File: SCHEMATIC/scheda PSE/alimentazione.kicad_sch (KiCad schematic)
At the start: 33 parts

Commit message: prova librerie
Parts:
- removed D?: S1B, symbol Device:D
- added D?: RBR1VWM30ATFTR, symbol Device:D_Schottky
- U?: farnell (none) -> 4144775
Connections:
- net +5V: now also D?.2 (A)
- net VOUT_5V: now also D?.1 (K)
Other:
- moved on the sheet: D?
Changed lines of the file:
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@@
   (junction (at 196.85 54.61) (diameter 0) (color 0 0 0 0)
   )
-  (junction (at 253.365 95.885) (diameter 0) (color 0 0 0 0)
+  (junction (at 249.555 95.885) (diameter 0) (color 0 0 0 0)
   )
   (junction (at 217.17 95.885) (diameter 0) (color 0 0 0 0)
@@
     (stroke (width 0) (type default) (color 0 0 0 0))
   )
-  (wire (pts (xy 254.635 95.885) (xy 253.365 95.885))
+  (wire (pts (xy 254.635 95.885) (xy 249.555 95.885))
     (stroke (width 0) (type default) (color 0 0 0 0))
   )
@@
     (stroke (width 0) (type default) (color 0 0 0 0))
   )
-  (wire (pts (xy 253.365 95.885) (xy 253.365 95.25))
+  (wire (pts (xy 249.555 95.885) (xy 249.555 95.25))
     (stroke (width 0) (type default) (color 0 0 0 0))
   )
@@
     (stroke (width 0) (type default) (color 0 0 0 0))
   )
-  (wire (pts (xy 67.945 95.885) (xy 73.66 95.885))
-    (stroke (width 0) (type default) (color 0 0 0 0))
-  )
-  (wire (pts (xy 247.015 95.885) (xy 253.365 95.885))
+  (wire (pts (xy 66.04 95.885) (xy 73.66 95.885))
+    (stroke (width 0) (type default) (color 0 0 0 0))
+  )
+  (wire (pts (xy 247.015 95.885) (xy 249.555 95.885))
     (stroke (width 0) (type default) (color 0 0 0 0))
   )
@@
     (stroke (width 0) (type default) (color 0 0 0 0))
   )
-  (wire (pts (xy 48.26 95.885) (xy 60.325 95.885))
+  (wire (pts (xy 48.26 95.885) (xy 58.42 95.885))
     (stroke (width 0) (type default) (color 0 0 0 0))
   )
@@
     (effects (font (size 1.27 1.27)) (justify left bottom))
   )
-  (label "VBUS" (at 83.82 52.705 0)
+  (label "VBUS" (at 84.455 52.705 0)
     (effects (font (size 1.27 1.27)) (justify left bottom))
   )
@@
     (effects (font (size 1.27 1.27)) (justify left bottom))
   )
-  (label "VIN_ POST_PPTC" (at 45.085 95.885 0)
+  (label "VIN_ POST_PPTC" (at 44.45 95.885 0)
     (effects (font (size 1.27 1.27)) (justify left bottom))
   )
@@
     (pin "1")
   )
-  (symbol (lib_id "power:+5V") (at 253.365 95.25 0) (unit 1)
-    (in_bom yes) (on_board yes) (fields_autoplaced)
-    (property "Reference" "#PWR0146" (id 0) (at 253.365 99.06 0)
-      (effects (font (size 1.27 1.27)) hide)
-    )
-    (property "Value" "+5V" (id 1) (at 253.365 91.6742 0))
-    (property "Footprint" "" (id 2) (at 253.365 95.25 0)
-      (effects (font (size 1.27 1.27)) hide)
-    )
-    (property "Datasheet" "" (id 3) (at 253.365 95.25 0)
+  (symbol (lib_id "power:+5V") (at 249.555 95.25 0) (unit 1)
+    (in_bom yes) (on_board yes) (fields_autoplaced)
+    (property "Reference" "#PWR0146" (id 0) (at 249.555 99.06 0)
+      (effects (font (size 1.27 1.27)) hide)
+    )
+    (property "Value" "+5V" (id 1) (at 249.555 91.6742 0))
+    (property "Footprint" "" (id 2) (at 249.555 95.25 0)
+      (effects (font (size 1.27 1.27)) hide)
+    )
+    (property "Datasheet" "" (id 3) (at 249.555 95.25 0)
       (effects (font (size 1.27 1.27)) hide)
     )
@@
     (pin "1")
   )
+  (symbol (lib_id "Device:D_Schottky") (at 258.445 95.885 180) (unit 1)
+    (in_bom yes) (on_board yes)
+    (property "Reference" "D?" (id 0) (at 258.445 93.345 0))
+    (property "Value" "RBR1VWM30ATFTR" (id 1) (at 260.35 99.06 0))
+    (property "Footprint" "" (id 2) (at 258.445 95.885 0)
+      (effects (font (size 1.27 1.27)) hide)
+    )
+    (property "Datasheet" "~" (id 3) (at 258.445 95.885 0)
+      (effects (font (size 1.27 1.27)) hide)
+    )
+    (pin "1")
+    (pin "2")
+  )
   (symbol (lib_id "power:GND") (at 177.165 113.665 0) (unit 1)
     (in_bom yes) (on_board yes) (fields_autoplaced)
@@
   (symbol (lib_id "Connector:TestPoint") (at 196.85 53.975 0) (unit 1)
     (in_bom yes) (on_board yes)
-    (property "Reference" "TP?" (id 0) (at 195.58 48.895 0)
-      (effects (font (size 1.27 1.27)) (justify left))
-    )
-    (property "Value" "3V3" (id 1) (at 195.58 46.3581 0)
+    (property "Reference" "TP?" (id 0) (at 198.12 50.8 0)
+      (effects (font (size 1.27 1.27)) (justify left))
+    )
+    (property "Value" "3V3" (id 1) (at 198.12 48.895 0)
       (effects (font (size 1.27 1.27)) (justify left))
     )
@@
       (effects (font (size 1.27 1.27)) hide)
     )
+    (property "farnell" "4144775" (id 4) (at 171.45 54.61 0)
+      (effects (font (size 1.27 1.27)) hide)
+    )
     (pin "1")
     (pin "2")
@@
     (pin "2")
   )
-  (symbol (lib_id "Device:D") (at 64.135 95.885 180) (unit 1)
-    (in_bom yes) (on_board yes) (fields_autoplaced)
-    (property "Reference" "D?" (id 0) (at 64.135 90.9152 0))
-    (property "Value" "S1B" (id 1) (at 64.135 93.4521 0))
-    (property "Footprint" "" (id 2) (at 64.135 95.885 0)
-      (effects (font (size 1.27 1.27)) hide)
-    )
-    (property "Datasheet" "~" (id 3) (at 64.135 95.885 0)
+  (symbol (lib_id "Device:D") (at 62.23 95.885 180) (unit 1)
+    (in_bom yes) (on_board yes)
+    (property "Reference" "D?" (id 0) (at 62.23 90.1731 0))
+    (property "Value" "S1B" (id 1) (at 62.23 92.71 0))
+    (property "Footprint" "" (id 2) (at 62.23 95.885 0)
+      (effects (font (size 1.27 1.27)) hide)
+    )
+    (property "Datasheet" "~" (id 3) (at 62.23 95.885 0)
       (effects (font (size 1.27 1.27)) hide)
     )
@@
   (symbol (lib_id "Device:Polyfuse") (at 40.64 95.885 90) (unit 1)
     (in_bom yes) (on_board yes)
-    (property "Reference" "F?" (id 0) (at 40.64 90.7882 90))
-    (property "Value" "2016L05MR" (id 1) (at 40.64 93.3251 90))
+    (property "Reference" "F?" (id 0) (at 40.64 90.1731 90))
+    (property "Value" "2016L05MR" (id 1) (at 40.64 92.71 90))
     (property "Footprint" "" (id 2) (at 45.72 94.615 0)
       (effects (font (size 1.27 1.27)) (justify left) hide)
@@
     (pin "1")
   )
-  (symbol (lib_id "Device:D") (at 258.445 95.885 180) (unit 1)
-    (in_bom yes) (on_board yes) (fields_autoplaced)
-    (property "Reference" "D?" (id 0) (at 258.445 90.9152 0))
-    (property "Value" "S1B" (id 1) (at 258.445 93.4521 0))
-    (property "Footprint" "" (id 2) (at 258.445 95.885 0)
-      (effects (font (size 1.27 1.27)) hide)
-    )
-    (property "Datasheet" "~" (id 3) (at 258.445 95.885 0)
-      (effects (font (size 1.27 1.27)) hide)
-    )
-    (pin "1")
-    (pin "2")
-  )
   (symbol (lib_id "Device:R") (at 247.015 109.855 0) (unit 1)

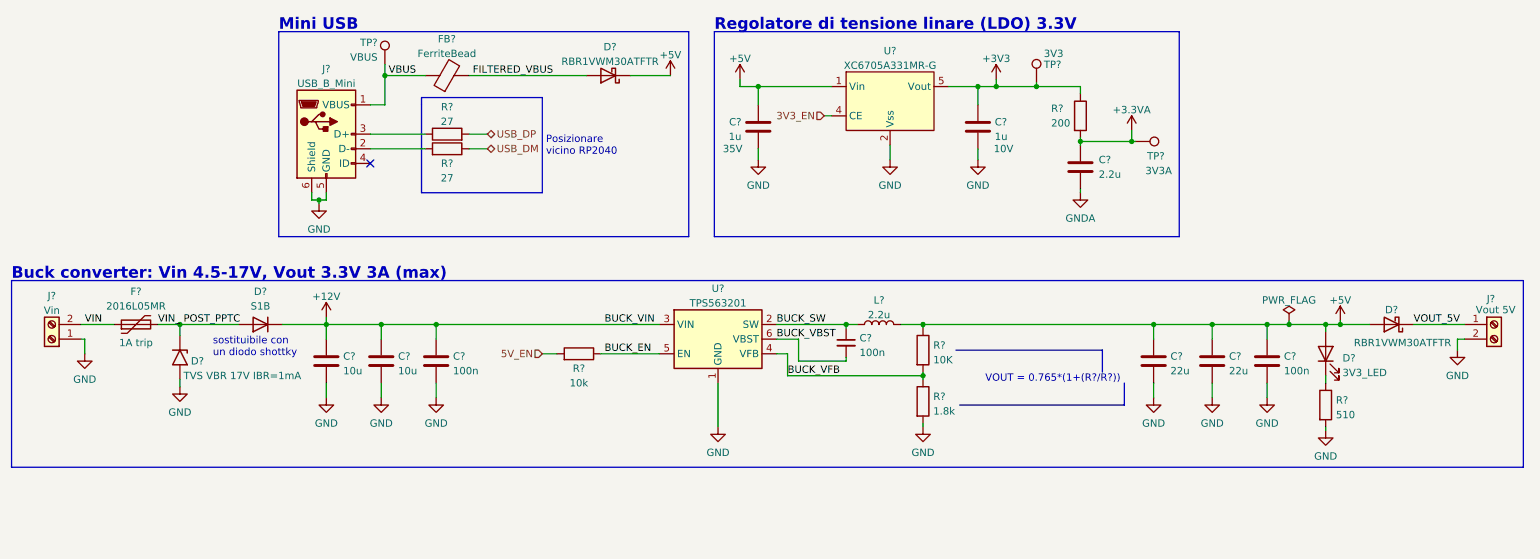
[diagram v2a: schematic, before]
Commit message: Aggiunti QUASI tutti i footprint
aggiunti quasi tutti i footprint dei componenti
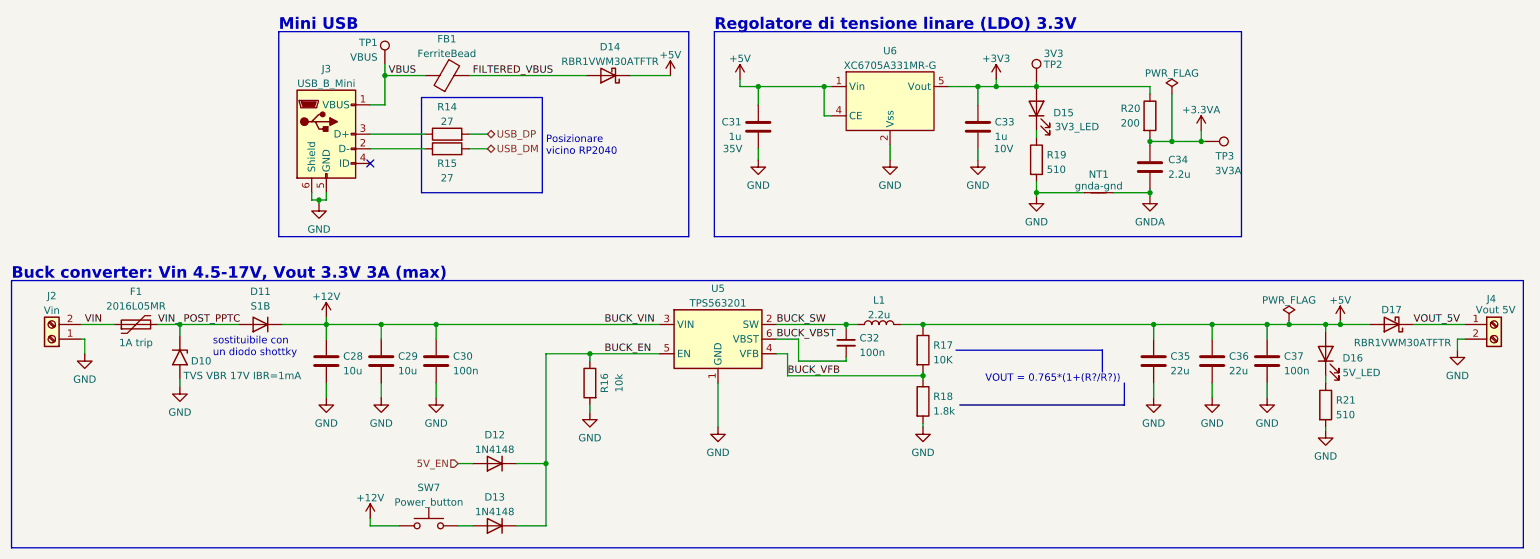
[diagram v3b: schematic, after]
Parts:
- added D12, D13: 1N4148, Diode_SMD:D_SOD-123, symbol Diode:1N4148
- added D15: 3V3_LED, LED_SMD:LED_0603_1608Metric, symbol Device:LED
- added NT1: gnda-gnd, NetTie:NetTie-2_SMD_Pad0.5mm, symbol Device:NetTie_2
- added R19: 510, Resistor_SMD:R_0603_1608Metric, symbol Device:R
- added SW7: Power_button, Button_Switch_THT:SW_PUSH_6mm_H5mm, symbol Switch:SW_Push
- C28, C29, C35, C36: renamed from C?; footprint (none) -> Capacitor_SMD:C_0805_2012Metric
- C30, C31, C32, C33, C34, C37: renamed from C?; footprint (none) -> Capacitor_SMD:C_0603_1608Metric
- D16: renamed from D?; value 3V3_LED -> 5V_LED; footprint (none) -> LED_SMD:LED_0603_1608Metric
- J2, J4: renamed from J?; footprint (none) -> TerminalBlock:TerminalBlock_bornier-2_P5.08mm
- R14, R15, R16, R17, R18, R20, R21: renamed from R?; footprint (none) -> Resistor_SMD:R_0603_1608Metric
- TP1, TP2, TP3: renamed from TP?; footprint (none) -> TestPoint:TestPoint_Loop_D2.50mm_Drill1.0mm_LowProfile
- gave numbers to parts that had none: 10
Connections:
- net 3V3_EN is gone; now on net +5V: U6.4 (CE)
- net +12V: now also SW7.1
- net +3V3: now also D15.2 (A)
- net 5V_EN: now also D12.2 (A); no longer R16.2
- net BUCK_EN: now also D12.1 (K), D13.1 (K)
- net GND: now also R16.2, NT1.1, R19.2
- net GNDA: now also NT1.2
- new net: D13.2 (A), SW7.2
- new net: D15.1 (K), R19.1
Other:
- moved on the sheet: C34, R16, R20, TP3

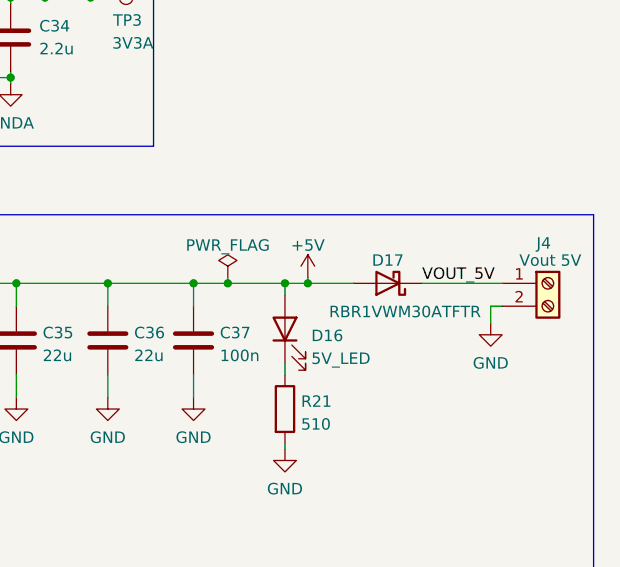
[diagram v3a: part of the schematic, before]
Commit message: iniziato il layout, posizionati componenti principali
incominciato il posizionamento dei componenti nel layout. Sono stati posizionati i componenti principali come led RGB, GPS, schermo, pulsanti vari, buzzer
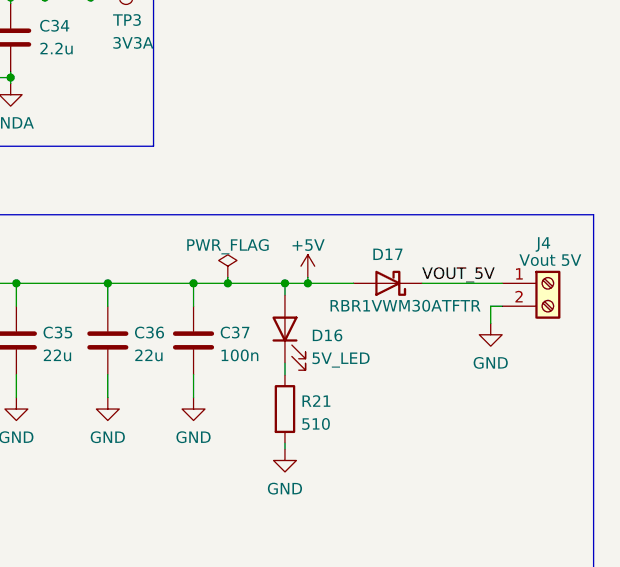
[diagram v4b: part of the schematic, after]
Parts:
- D10: footprint Diode_THT:D_DO-201AE_P15.24mm_Horizontal -> Diode_SMD:D_SMA; mouser (none) -> 576-SMAJ15A
- D11: footprint (none) -> Diode_SMD:D_SMA; farnell (none) -> 2675037
- D14, D17: footprint (none) -> Diode_SMD:D_SOD-123; farnell (none) -> 2311223
- D15, D16: footprint LED_SMD:LED_0603_1608Metric -> LED_SMD:LED_0805_2012Metric
- F1: footprint (none) -> Fuse:Fuse_1206_3216Metric; farnell (none) -> 1652159
- FB1: footprint (none) -> Capacitor_SMD:C_0805_2012Metric; farnell (none) -> 1515661
- J3: footprint (none) -> _PSE:USB mini
- L1: footprint (none) -> _PSE:IHLP1212BZER2R2M11; farnell (none) -> 2056527
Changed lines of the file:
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@@
     (pin "1")
-  )
-  (symbol (lib_id "Device:D_Schottky") (at 258.445 95.885 180) (unit 1)
-    (in_bom yes) (on_board yes)
-    (property "Reference" "D17" (id 0) (at 258.445 93.345 0))
-    (property "Value" "RBR1VWM30ATFTR" (id 1) (at 260.35 99.06 0))
-    (property "Footprint" "" (id 2) (at 258.445 95.885 0)
-      (effects (font (size 1.27 1.27)) hide)
-    )
-    (property "Datasheet" "~" (id 3) (at 258.445 95.885 0)
-      (effects (font (size 1.27 1.27)) hide)
-    )
-    (pin "1")
-    (pin "2")
   )
   (symbol (lib_id "power:GND") (at 177.165 113.665 0) (unit 1)
@@
     (pin "1")
   )
+  (symbol (lib_id "Device:D_Schottky") (at 258.445 95.885 180) (unit 1)
+    (in_bom yes) (on_board yes)
+    (property "Reference" "D17" (id 0) (at 258.445 92.71 0))
+    (property "Value" "RBR1VWM30ATFTR" (id 1) (at 260.35 98.425 0))
+    (property "Footprint" "Diode_SMD:D_SOD-123" (id 2) (at 258.445 95.885 0)
+      (effects (font (size 1.27 1.27)) hide)
+    )
+    (property "Datasheet" "https://4donline.ihs.com/images/VipMasterIC/IC/NEXP/NEXP-S-A0003060256/NEXP-S-A0003059924-1.pdf?hkey=6D3A4C79FDBF58556ACFDE234799DDF0" (id 3) (at 258.445 95.885 0)
+      (effects (font (size 1.27 1.27)) hide)
+    )
+    (property "farnell" "2311223" (id 4) (at 258.445 95.885 0)
+      (effects (font (size 1.27 1.27)) hide)
+    )
+    (pin "1")
+    (pin "2")
+  )
   (symbol (lib_id "Connector:Screw_Terminal_01x02") (at 276.225 95.885 0) (unit 1)
     (in_bom yes) (on_board yes)
@@
     (property "Reference" "D11" (id 0) (at 62.23 90.1731 0))
     (property "Value" "S1B" (id 1) (at 62.23 92.71 0))
-    (property "Footprint" "" (id 2) (at 62.23 95.885 0)
-      (effects (font (size 1.27 1.27)) hide)
-    )
-    (property "Datasheet" "~" (id 3) (at 62.23 95.885 0)
+    (property "Footprint" "Diode_SMD:D_SMA" (id 2) (at 62.23 95.885 0)
+      (effects (font (size 1.27 1.27)) hide)
+    )
+    (property "Datasheet" "https://www.farnell.com/datasheets/2863963.pdf" (id 3) (at 62.23 95.885 0)
+      (effects (font (size 1.27 1.27)) hide)
+    )
+    (property "farnell" "2675037" (id 4) (at 62.23 95.885 0)
       (effects (font (size 1.27 1.27)) hide)
     )
@@
     (property "Reference" "F1" (id 0) (at 40.64 90.1731 90))
     (property "Value" "2016L05MR" (id 1) (at 40.64 92.71 90))
-    (property "Footprint" "" (id 2) (at 45.72 94.615 0)
+    (property "Footprint" "Fuse:Fuse_1206_3216Metric" (id 2) (at 45.72 94.615 0)
       (effects (font (size 1.27 1.27)) (justify left) hide)
     )
-    (property "Datasheet" "~" (id 3) (at 40.64 95.885 0)
+    (property "Datasheet" "https://www.farnell.com/datasheets/2360307.pdf" (id 3) (at 40.64 95.885 0)
       (effects (font (size 1.27 1.27)) hide)
     )
     (property "Rating" "1A trip" (id 4) (at 40.64 99.06 90))
+    (property "farnell" "1652159" (id 5) (at 40.64 95.885 90)
+      (effects (font (size 1.27 1.27)) hide)
+    )
     (pin "1")
     (pin "2")
@@
       (effects (font (size 1.27 1.27)) (justify right))
     )
-    (property "Footprint" "LED_SMD:LED_0603_1608Metric" (id 2) (at 196.85 58.42 0)
+    (property "Footprint" "LED_SMD:LED_0805_2012Metric" (id 2) (at 196.85 58.42 0)
       (effects (font (size 1.27 1.27)) hide)
     )
@@
     (property "Reference" "L1" (id 0) (at 169.545 91.6772 90))
     (property "Value" "2.2u" (id 1) (at 169.545 94.2141 90))
-    (property "Footprint" "" (id 2) (at 169.545 95.885 0)
-      (effects (font (size 1.27 1.27)) hide)
-    )
-    (property "Datasheet" "~" (id 3) (at 169.545 95.885 0)
+    (property "Footprint" "_PSE:IHLP1212BZER2R2M11" (id 2) (at 169.545 95.885 0)
+      (effects (font (size 1.27 1.27)) hide)
+    )
+    (property "Datasheet" "https://www.farnell.com/datasheets/3707258.pdf" (id 3) (at 169.545 95.885 0)
+      (effects (font (size 1.27 1.27)) hide)
+    )
+    (property "farnell" "2056527" (id 4) (at 169.545 95.885 90)
       (effects (font (size 1.27 1.27)) hide)
     )
@@
       (effects (font (size 1.27 1.27)) (justify right))
     )
-    (property "Footprint" "LED_SMD:LED_0603_1608Metric" (id 2) (at 247.015 100.965 0)
+    (property "Footprint" "LED_SMD:LED_0805_2012Metric" (id 2) (at 247.015 100.965 0)
       (effects (font (size 1.27 1.27)) hide)
     )
@@
     (property "Reference" "J3" (id 0) (at 73.66 51.5452 0))
     (property "Value" "USB_B_Mini" (id 1) (at 73.66 54.0821 0))
-    (property "Footprint" "" (id 2) (at 77.47 64.135 0)
+    (property "Footprint" "_PSE:USB mini" (id 2) (at 77.47 64.135 0)
       (effects (font (size 1.27 1.27)) hide)
     )
@@
     (property "Reference" "FB1" (id 0) (at 94.5642 46.3636 90))
     (property "Value" "FerriteBead" (id 1) (at 94.5642 48.9005 90))
-    (property "Footprint" "" (id 2) (at 94.615 54.483 90)
-      (effects (font (size 1.27 1.27)) hide)
-    )
-    (property "Datasheet" "~" (id 3) (at 94.615 52.705 0)
+    (property "Footprint" "Capacitor_SMD:C_0805_2012Metric" (id 2) (at 94.615 54.483 90)
+      (effects (font (size 1.27 1.27)) hide)
+    )
+    (property "Datasheet" "https://it.farnell.com/murata/blm21pg221sn1d/ferrite-perlina-0805-0-045ohm/dp/1515661?st=blm21" (id 3) (at 94.615 52.705 0)
+      (effects (font (size 1.27 1.27)) hide)
+    )
+    (property "farnell" "1515661" (id 4) (at 94.615 52.705 90)
       (effects (font (size 1.27 1.27)) hide)
     )
@@
     (property "Reference" "D14" (id 0) (at 122.8725 47.7352 0))
     (property "Value" "RBR1VWM30ATFTR" (id 1) (at 122.8725 50.2721 0))
-    (property "Footprint" "" (id 2) (at 122.555 52.705 0)
-      (effects (font (size 1.27 1.27)) hide)
-    )
-    (property "Datasheet" "~" (id 3) (at 122.555 52.705 0)
+    (property "Footprint" "Diode_SMD:D_SOD-123" (id 2) (at 122.555 52.705 0)
+      (effects (font (size 1.27 1.27)) hide)
+    )
+    (property "Datasheet" "https://4donline.ihs.com/images/VipMasterIC/IC/NEXP/NEXP-S-A0003060256/NEXP-S-A0003059924-1.pdf?hkey=6D3A4C79FDBF58556ACFDE234799DDF0" (id 3) (at 122.555 52.705 0)
+      (effects (font (size 1.27 1.27)) hide)
+    )
+    (property "farnell" "2311223" (id 4) (at 122.555 52.705 0)
       (effects (font (size 1.27 1.27)) hide)
     )
@@
       (effects (font (size 1.27 1.27)) (justify left))
     )
-    (property "Footprint" "Diode_THT:D_DO-201AE_P15.24mm_Horizontal" (id 2) (at 43.18 101.6 0)
-      (effects (font (size 1.27 1.27)) hide)
-    )
-    (property "Datasheet" "https://www.vishay.com/docs/88301/15ke.pdf" (id 3) (at 48.26 100.33 0)
-      (effects (font (size 1.27 1.27)) hide)
-    )
+    (property "Footprint" "Diode_SMD:D_SMA" (id 2) (at 43.18 101.6 0)
+      (effects (font (size 1.27 1.27)) hide)
+    )
+    (property "Datasheet" "https://www.mouser.it/datasheet/2/240/Littelfuse_TVS_Diode_SMAJ_Datasheet_pdf-540740.pdf" (id 3) (at 48.26 100.33 0)
+      (effects (font (size 1.27 1.27)) hide)
+    )
+    (property "mouser" "576-SMAJ15A" (id 4) (at 48.26 101.6 90)
+      (effects (font (size 1.27 1.27)) hide)
+    )
